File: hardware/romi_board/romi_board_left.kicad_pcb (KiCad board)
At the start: 2 copper layers, 99.1 x 66 mm, 33 parts, among them J1 Conn_01x14, J2 Conn_01x14, J3 Conn_01x04, SW1 SW_SPST, U1 Teensy4.0

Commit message: Initial version of schematics and boards.
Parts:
- removed C_LEFT1: Conn_01x07, Connector_PinHeader_2.54mm:PinHeader_1x06_P2.54mm_Vertical
- removed D1: LED, LED_THT:LED_D5.0mm
- removed DRV_LEFT1, DRV_RIGHT1: TB9051FTG, teensy:TB9051FTG_db
- removed ENCODER_RIGHT1: Conn_01x06, Connector_PinHeader_2.54mm:PinHeader_1x06_P2.54mm_Vertical
- removed I2C_ACC1, I2C_ACC2, I2C_ACC3, I2C_ACC4, J3, ULTRASONIC1: Conn_01x04, Connector_PinHeader_2.54mm:PinHeader_1x04_P2.54mm_Vertical
- removed IMU-9250: Conn_01x04, teensy:MPU9250_BB
- removed J2: Conn_01x14, Connector_PinHeader_2.54mm:PinHeader_1x14_P2.54mm_Vertical
- removed JP1, JP2, JP3: SolderJumper_2_Open, Jumper:SolderJumper-2_P1.3mm_Open_RoundedPad1.0x1.5mm
- removed JP4, JP5: SolderJumper_2_Bridged, Jumper:SolderJumper-2_P1.3mm_Bridged_RoundedPad1.0x1.5mm
- removed PI1: RASPBERRY_PI_GPIO, Connector_PinHeader_2.54mm:PinHeader_2x05_P2.54mm_Vertical
- removed PWR1: Conn_02x10_Counter_Clockwise, Connector_PinHeader_2.54mm:PinHeader_2x10_P2.54mm_Vertical
- removed R1, R2, R3, R4, R5, R8, R9: R_US, Resistor_THT:R_Axial_DIN0309_L9.0mm_D3.2mm_P2.54mm_Vertical
- removed R6, R7: R_Small_US, Resistor_THT:R_Axial_DIN0309_L9.0mm_D3.2mm_P2.54mm_Vertical
- removed REG_5V1: D24V22F5, teensy:D24V2F5_bb
- removed SW1: SW_SPST, Connector_PinHeader_2.54mm:PinHeader_1x02_P2.54mm_Vertical
- removed U1: Teensy4.0, teensy:Teensy40_SMT
- added B2M1: BTAB, teensy:romi_battery_tab, F.Cu at (73.3, 112.7)
- added B2P1: BTAB, teensy:romi_battery_tab, F.Cu at (73.3, 98.2)
- added B4M1: BTAB, teensy:romi_battery_tab, F.Cu at (47.7, 144.1)
- added B4P1: BTAB, teensy:romi_battery_tab, F.Cu at (47.7, 129.6)
- added C_LEFTx1: Conn_01x07, Connector_PinHeader_2.54mm:PinHeader_1x06_P2.54mm_Vertical, F.Cu at (69.2, 101.3)
- added ENCODER_LEFT1: Conn_01x06, Connector_PinHeader_2.54mm:PinHeader_1x06_P2.54mm_Vertical, F.Cu at (64.9, 101.3)
- added REF**: MountingHole_2.5mm, MountingHole:MountingHole_2.5mm, F.Cu at (61.4, 93.1)
- added REF**: MountingHole_2.5mm, MountingHole:MountingHole_2.5mm, F.Cu at (56.4, 124.6)
- added REF**: MountingHole_2.5mm, MountingHole:MountingHole_2.5mm, F.Cu at (81.4, 93.1)
- added REF**: MountingHole_2.5mm, MountingHole:MountingHole_2.5mm, F.Cu at (56.4, 149.1)
- J1: value Conn_01x14 -> Conn_01x04; footprint Connector_PinHeader_2.54mm:PinHeader_1x14_P2.54mm_Vertical -> Connector_PinHeader_2.54mm:PinHeader_1x04_P2.54mm_Vertical
- moved J1 67.1 mm to (69.2, 129.3), turned to 270 degrees
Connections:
- J1 pad 1: GND -> +BATT
- J1 pad 2: /TSY_RX -> +BATT
- J1 pad 3: /TSY_TX -> /VBAT_MID
- J1 pad 4: /XD_EN -> GND
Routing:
- net +5V: track 318.9 -> 0.00 mm, vias 4 -> 0
- net +3V3: track 146.9 -> 0.00 mm, vias 4 -> 0
- net +VSW: track 129.1 -> 0.00 mm
- net /I2C2_SDA: track 97.3 -> 0.00 mm, vias 3 -> 0
- net /LD_PWM1: track 87.3 -> 0.00 mm, vias 3 -> 0
- net /LENCA: track 83.1 -> 0.00 mm, vias 3 -> 0
- net /I2C1_SCL: track 81.9 -> 0.00 mm, vias 1 -> 0
- net /I2C1_SDA: track 81.6 -> 0.00 mm, vias 2 -> 0
- net /LENCB: track 81.5 -> 0.00 mm, vias 3 -> 0
- net /I2C2_SCL: track 81.2 -> 0.00 mm
- net /US_TRIG: track 79.7 -> 0.00 mm, vias 2 -> 0
- net /LD_OCM: track 68.9 -> 0.00 mm, vias 4 -> 0
- net /XD_EN: track 67.6 -> 0.00 mm, vias 3 -> 0
- net /LD_PWM2: track 61.5 -> 0.00 mm, vias 2 -> 0
- net /RENCA: track 55.9 -> 0.00 mm, vias 2 -> 0
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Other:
- board size 99.1 x 66 mm -> 38 x 60 mm
- net class Motor removed
- net class PWR added: clearance 0.6, trace_width 2, via_dia 0.8, via_drill 0.4
- net class Supply removed

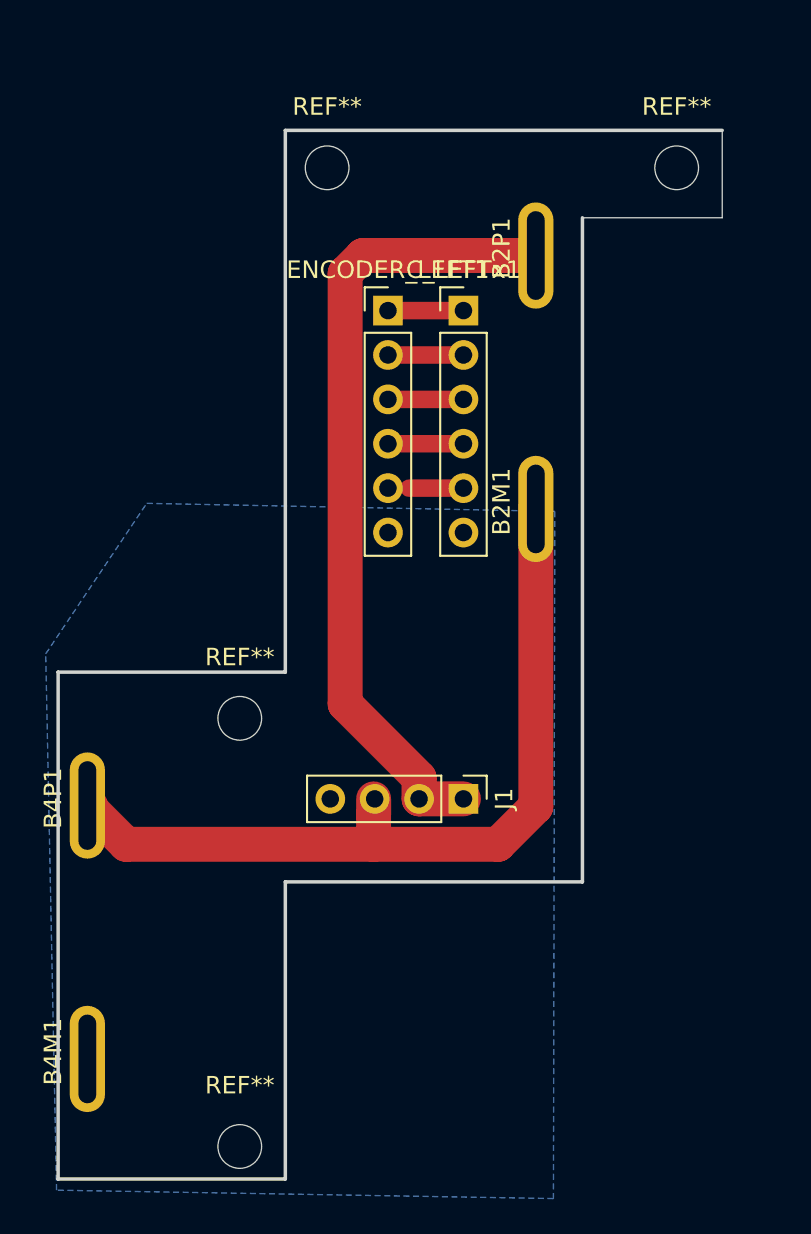
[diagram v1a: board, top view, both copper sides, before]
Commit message: flip the left motor encorder connector the right way round.
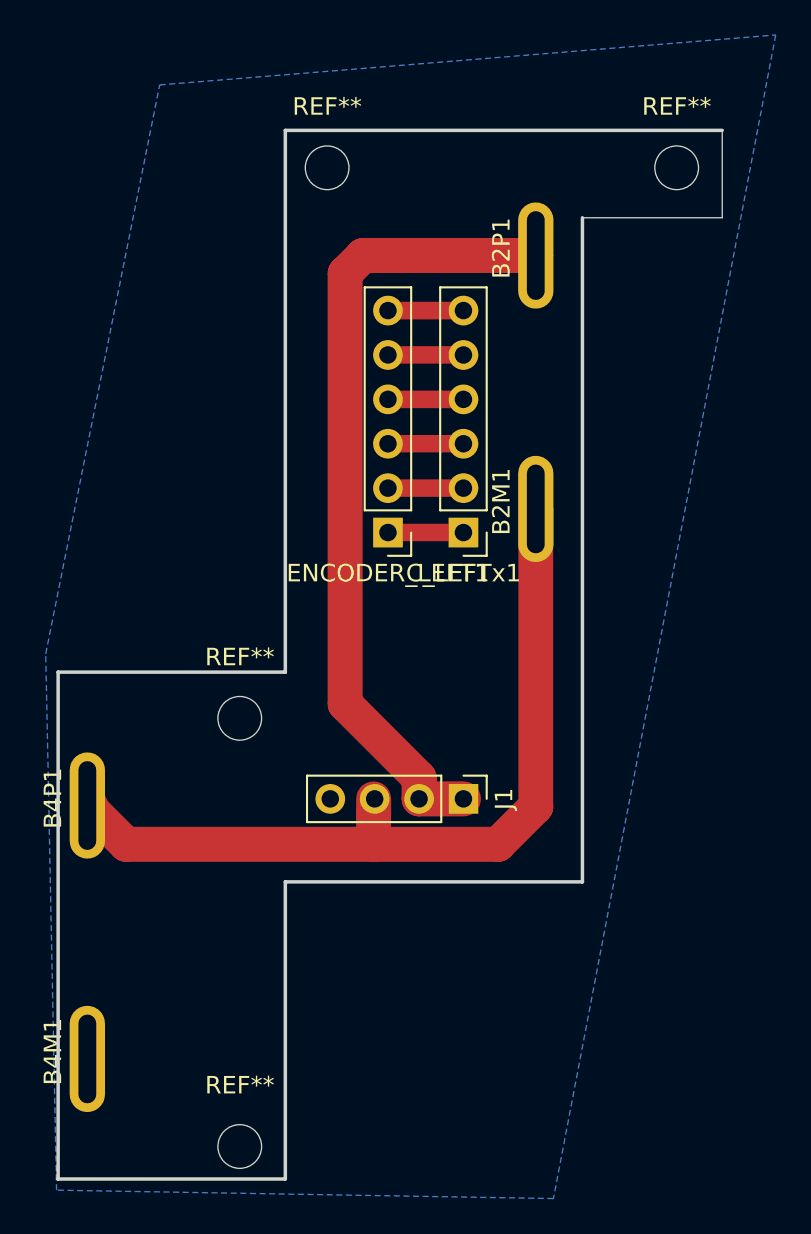
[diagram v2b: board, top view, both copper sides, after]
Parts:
- moved C_LEFTx1 12.7 mm to (69.2, 114.0), turned to 180 degrees
- moved ENCODER_LEFT1 12.7 mm to (64.9, 114.0), turned to 180 degrees
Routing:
- net GND: track 0.00 -> 4.32 mm
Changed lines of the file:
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@@
   )
   (setup
-    (last_trace_width 0.25)
+    (last_trace_width 1)
+    (user_trace_width 1)
+    (user_trace_width 2)
     (trace_clearance 0.2)
     (zone_clearance 0.508)
@@
   )
   (module Connector_PinHeader_2.54mm:PinHeader_1x06_P2.54mm_Vertical (layer F.Cu)
-    (at 64.872122 101.310976)
+    (at 64.872122 114.010976 180)
     (descr "Through hole straight pin header, 1x06, 2.54mm pitch, single row")
     (tags "Through hole pin header THT 1x06 2.54mm single row")
@@
       (effects (font (size 1 1) (thickness 0.15)))
     )
-    (pad 1 thru_hole rect (at 0 0) (size 1.7 1.7) (drill 1) (layers *.Cu *.Mask)
+    (pad 1 thru_hole rect (at 0 0 180) (size 1.7 1.7) (drill 1) (layers *.Cu *.Mask)
       (net 4 /LM1x))
-    (pad 2 thru_hole oval (at 0 2.54) (size 1.7 1.7) (drill 1) (layers *.Cu *.Mask)
+    (pad 2 thru_hole oval (at 0 2.54 180) (size 1.7 1.7) (drill 1) (layers *.Cu *.Mask)
       (net 5 /LM2x))
-    (pad 3 thru_hole oval (at 0 5.08) (size 1.7 1.7) (drill 1) (layers *.Cu *.Mask)
+    (pad 3 thru_hole oval (at 0 5.08 180) (size 1.7 1.7) (drill 1) (layers *.Cu *.Mask)
       (net 6 /L5V))
-    (pad 4 thru_hole oval (at 0 7.62) (size 1.7 1.7) (drill 1) (layers *.Cu *.Mask)
+    (pad 4 thru_hole oval (at 0 7.62 180) (size 1.7 1.7) (drill 1) (layers *.Cu *.Mask)
       (net 7 /LENCAx))
-    (pad 5 thru_hole oval (at 0 10.16) (size 1.7 1.7) (drill 1) (layers *.Cu *.Mask)
+    (pad 5 thru_hole oval (at 0 10.16 180) (size 1.7 1.7) (drill 1) (layers *.Cu *.Mask)
       (net 8 /LENCBx))
-    (pad 6 thru_hole oval (at 0 12.7) (size 1.7 1.7) (drill 1) (layers *.Cu *.Mask)
+    (pad 6 thru_hole oval (at 0 12.7 180) (size 1.7 1.7) (drill 1) (layers *.Cu *.Mask)
       (net 3 GND))
     (model ${KISYS3DMOD}/Connector_PinHeader_2.54mm.3dshapes/PinHeader_1x06_P2.54mm_Vertical.wrl
@@
   )
   (module Connector_PinHeader_2.54mm:PinHeader_1x06_P2.54mm_Vertical (layer F.Cu)
-    (at 69.192122 101.310976)
+    (at 69.192122 114.010976 180)
     (descr "Through hole straight pin header, 1x06, 2.54mm pitch, single row")
     (tags "Through hole pin header THT 1x06 2.54mm single row")
@@
       (effects (font (size 1 1) (thickness 0.15)))
     )
-    (pad 1 thru_hole rect (at 0 0) (size 1.7 1.7) (drill 1) (layers *.Cu *.Mask)
+    (pad 1 thru_hole rect (at 0 0 180) (size 1.7 1.7) (drill 1) (layers *.Cu *.Mask)
       (net 4 /LM1x))
-    (pad 2 thru_hole oval (at 0 2.54) (size 1.7 1.7) (drill 1) (layers *.Cu *.Mask)
+    (pad 2 thru_hole oval (at 0 2.54 180) (size 1.7 1.7) (drill 1) (layers *.Cu *.Mask)
       (net 5 /LM2x))
-    (pad 3 thru_hole oval (at 0 5.08) (size 1.7 1.7) (drill 1) (layers *.Cu *.Mask)
+    (pad 3 thru_hole oval (at 0 5.08 180) (size 1.7 1.7) (drill 1) (layers *.Cu *.Mask)
       (net 6 /L5V))
-    (pad 4 thru_hole oval (at 0 7.62) (size 1.7 1.7) (drill 1) (layers *.Cu *.Mask)
+    (pad 4 thru_hole oval (at 0 7.62 180) (size 1.7 1.7) (drill 1) (layers *.Cu *.Mask)
       (net 7 /LENCAx))
-    (pad 5 thru_hole oval (at 0 10.16) (size 1.7 1.7) (drill 1) (layers *.Cu *.Mask)
+    (pad 5 thru_hole oval (at 0 10.16 180) (size 1.7 1.7) (drill 1) (layers *.Cu *.Mask)
       (net 8 /LENCBx))
-    (pad 6 thru_hole oval (at 0 12.7) (size 1.7 1.7) (drill 1) (layers *.Cu *.Mask)
+    (pad 6 thru_hole oval (at 0 12.7 180) (size 1.7 1.7) (drill 1) (layers *.Cu *.Mask)
       (net 3 GND))
     (model ${KISYS3DMOD}/Connector_PinHeader_2.54mm.3dshapes/PinHeader_1x06_P2.54mm_Vertical.wrl
@@
   (segment (start 73.332122 98.160976) (end 63.44212 98.160976) (width 2) (layer F.Cu) (net 2))
   (segment (start 66.652122 129.250976) (end 69.192122 129.250976) (width 2) (layer F.Cu) (net 2))
-  (segment (start 64.872122 101.310976) (end 69.192122 101.310976) (width 1) (layer F.Cu) (net 4))
-  (segment (start 64.872122 103.850976) (end 69.192122 103.850976) (width 1) (layer F.Cu) (net 5))
-  (segment (start 64.872122 106.390976) (end 69.192122 106.390976) (width 1) (layer F.Cu) (net 6))
-  (segment (start 64.872122 108.930976) (end 69.192122 108.930976) (width 1) (layer F.Cu) (net 7))
-  (segment (start 66.074203 111.470976) (end 69.192122 111.470976) (width 1) (layer F.Cu) (net 8))
-  (segment (start 64.872122 111.470976) (end 66.074203 111.470976) (width 0.25) (layer F.Cu) (net 8))
+  (segment (start 69.192122 101.310976) (end 64.872122 101.310976) (width 1) (layer F.Cu) (net 3))
+  (segment (start 64.872122 114.010976) (end 69.192122 114.010976) (width 1) (layer F.Cu) (net 4))
+  (segment (start 69.192122 111.470976) (end 64.872122 111.470976) (width 1) (layer F.Cu) (net 5))
+  (segment (start 64.872122 108.930976) (end 69.192122 108.930976) (width 1) (layer F.Cu) (net 6))
+  (segment (start 69.192122 106.390976) (end 64.872122 106.390976) (width 1) (layer F.Cu) (net 7))
+  (segment (start 64.872122 103.850976) (end 69.192122 103.850976) (width 1) (layer F.Cu) (net 8))
   (zone (net 3) (net_name GND) (layer B.Cu) (hatch edge 0.508)
     (connect_pads (clearance 0.508))
@@
     (polygon
       (pts
-        (xy 74.34 152.12) (xy 45.91 151.64) (xy 45.29 120.95) (xy 51.07 112.34) (xy 74.42 112.8)
+        (xy 74.34 152.12) (xy 45.91 151.64) (xy 45.29 120.95) (xy 51.81 88.4) (xy 87.06 85.54)
       )
     )
